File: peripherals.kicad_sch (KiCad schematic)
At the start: 71 parts, among them J801 TC2050-IDC-NL, J803 533980471, Q801 BSS138W-7-F, Q802 BSS138W-7-F, Q803 BSS138W-7-F, Q804 BSS138W-7-F, U801 TXB0108DQSR, U802 TXB0108DQSR, U803 PCAL6416AHF, U804 TXB0108DQSR, U805 AP22615, U806 AP22615, U807 74LVC1T45GM

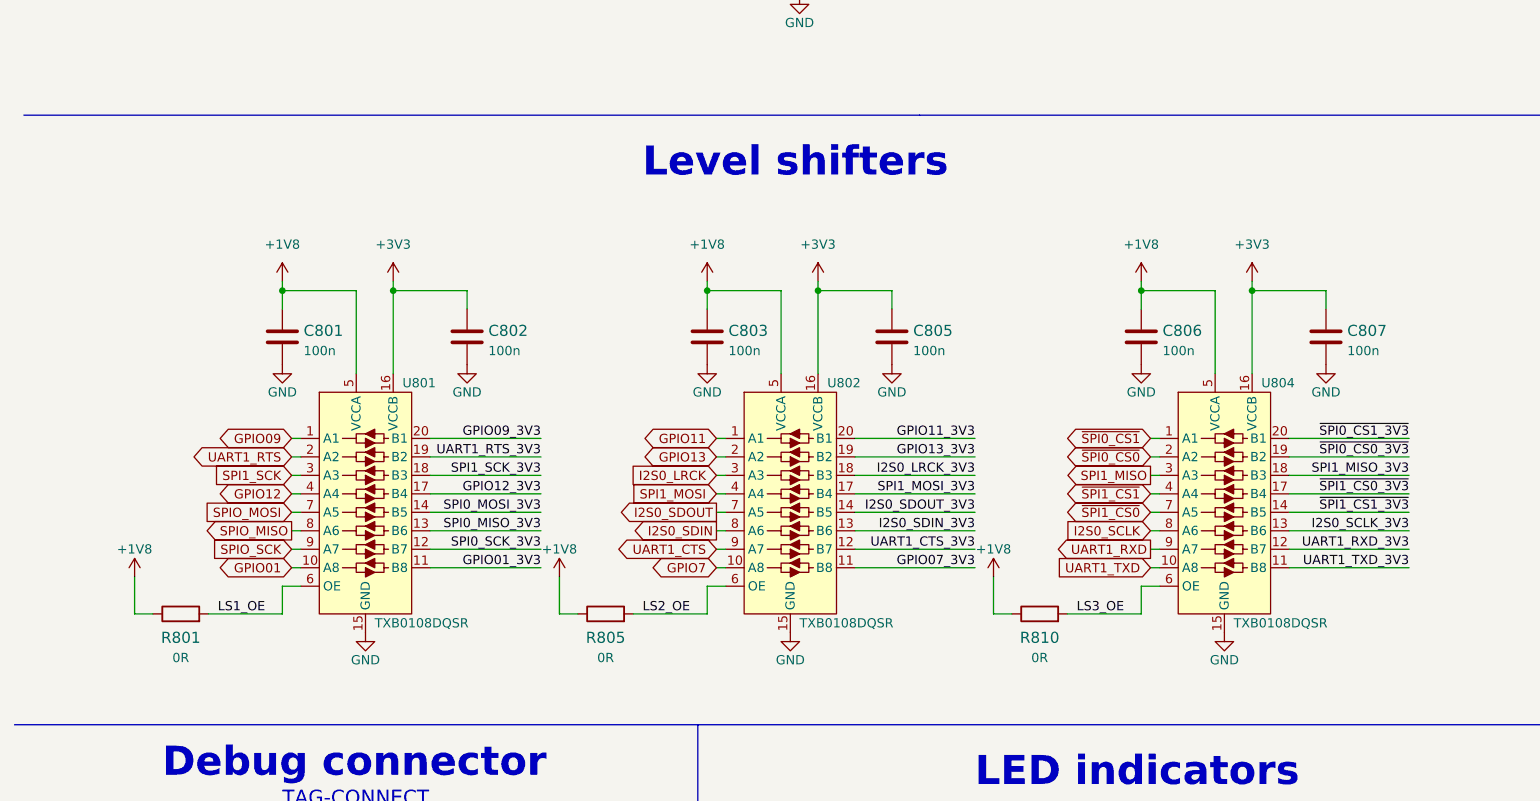
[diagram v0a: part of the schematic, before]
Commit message: Remove unused level shifters
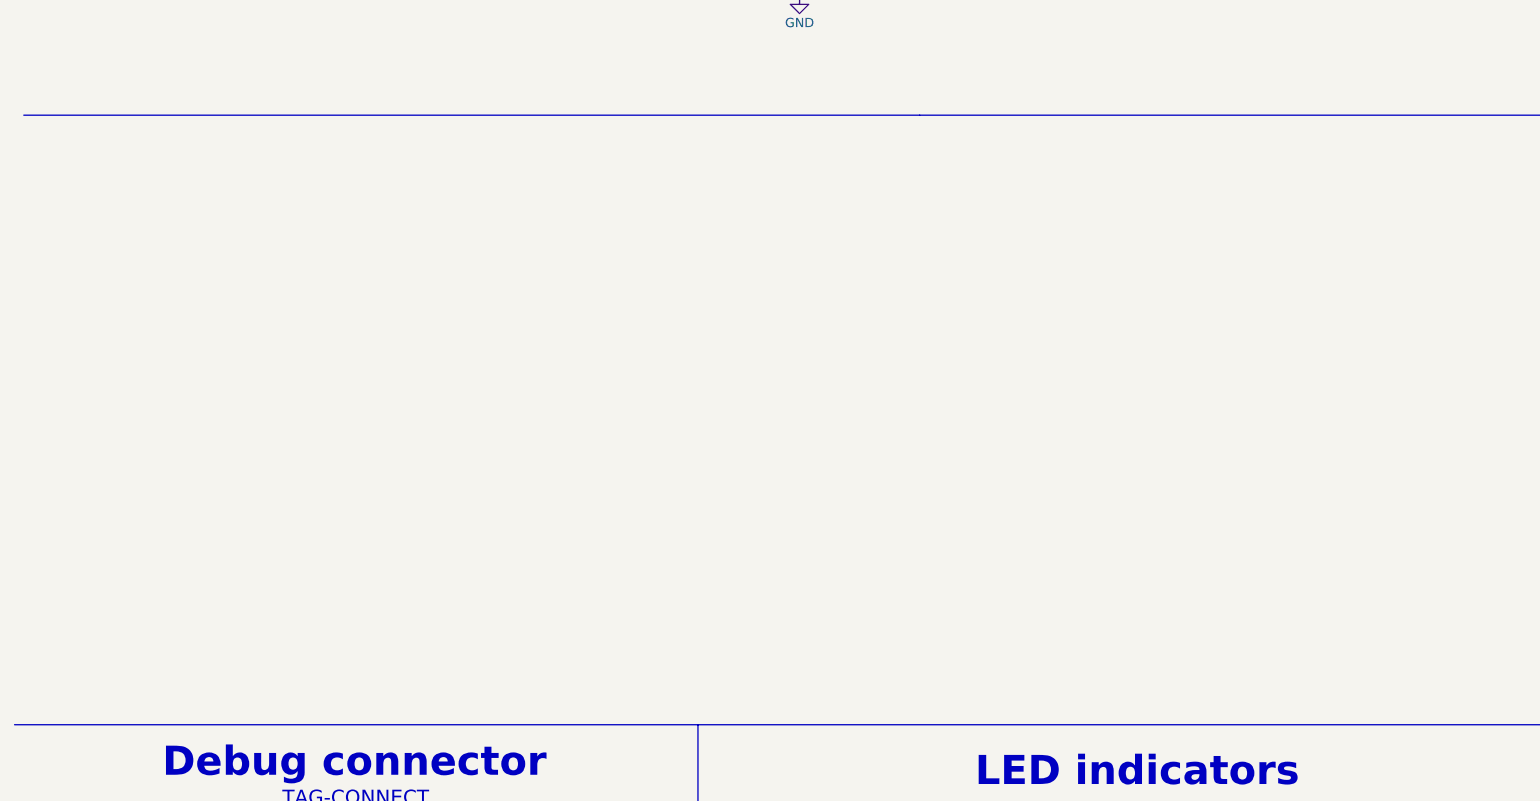
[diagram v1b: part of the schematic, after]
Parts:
- removed C801, C802, C803, C805, C806, C807: C_100n_0402, antmicro-footprints:0402-cap, symbol antmicroCapacitors0402:C_100n_0402
- removed R801, R805, R810: R_0R_0402, antmicro-footprints:0402-res, symbol antmicroResistors0402:R_0R_0402
- removed U801, U802, U804: TXB0108DQSR, antmicro-footprints:USON-20_2x4mm_P0.4mm, symbol antmicroLogicTranslatorsLevelShifters:TXB0108DQSR
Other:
- note removed: "Level shifters"

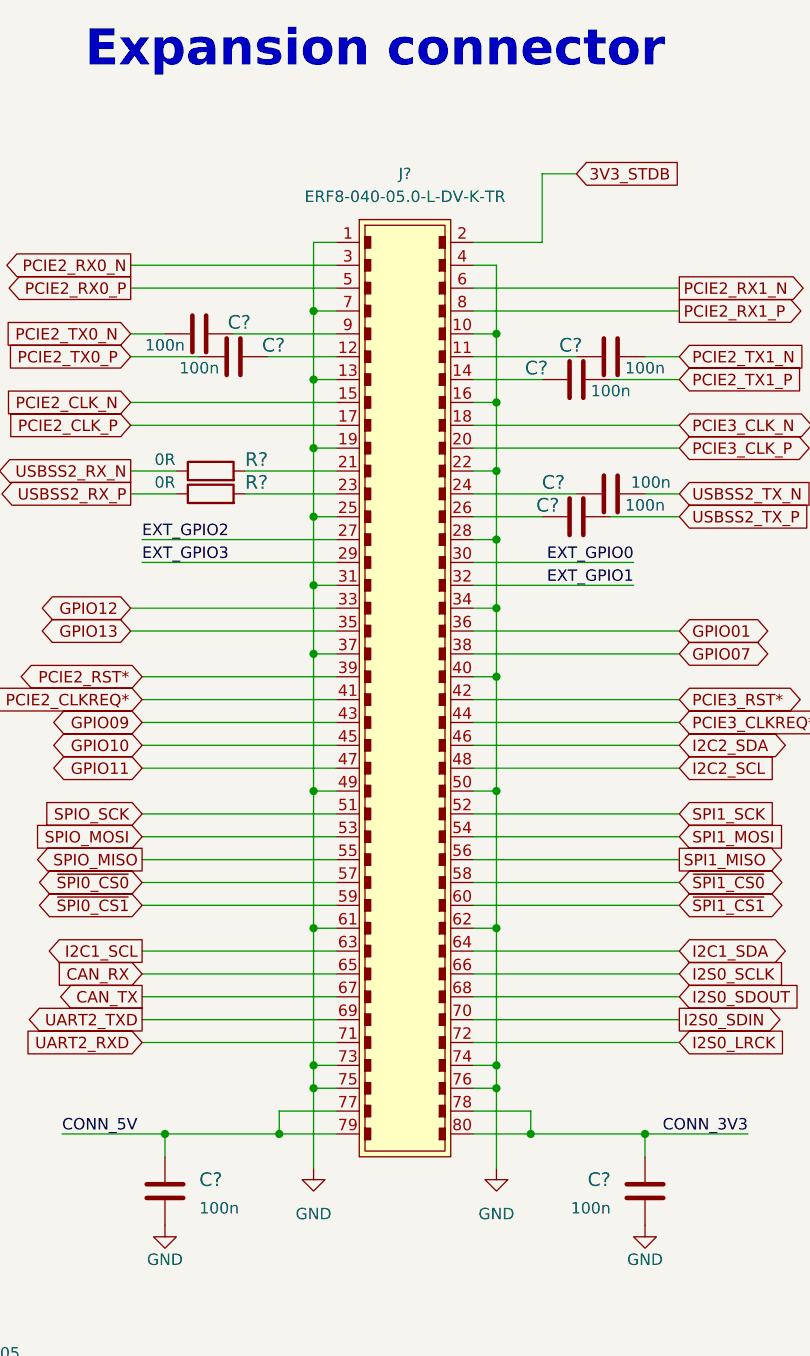
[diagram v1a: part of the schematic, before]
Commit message: Update expansion connector symbol, iport it to PCB
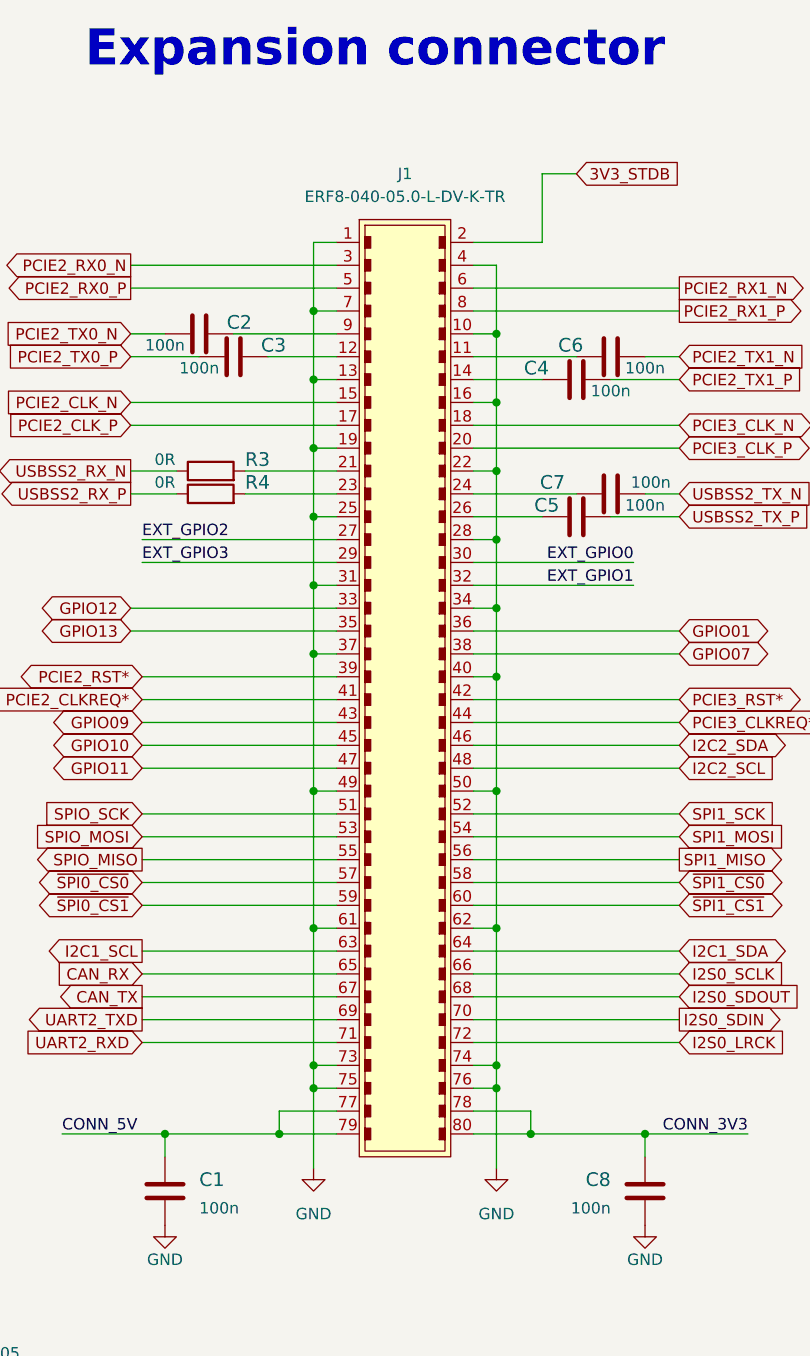
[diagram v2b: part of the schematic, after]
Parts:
- J1: renamed from J?; footprint antmicro-footprints:ERF8-XXX-XX.X-X-DV-XXXX-TR -> antmicro-footprints:ERF8-040-XX.X-X-DV-XX; Manufacturer (none) -> Samtec
- gave numbers to parts that had none: 10
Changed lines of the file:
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@@
   (symbol (lib_id "antmicroCapacitors0402:C_100n_0402") (at 341.63 71.12 270) (mirror x) (unit 1)
     (in_bom yes) (on_board yes)
-    (property "Reference" "C?" (id 0) (at 339.725 69.85 90)
+    (property "Reference" "C5" (id 0) (at 339.725 69.85 90)
       (effects (font (size 1.524 1.524)) (justify right))
     )
@@
   (symbol (lib_id "antmicroCapacitors0402:C_100n_0402") (at 341.63 55.88 270) (mirror x) (unit 1)
     (in_bom yes) (on_board yes)
-    (property "Reference" "C?" (id 0) (at 337.185 54.61 90)
+    (property "Reference" "C4" (id 0) (at 337.185 54.61 90)
       (effects (font (size 1.524 1.524)))
     )
@@
   (symbol (lib_id "antmicroCapacitors0402:C_100n_0402") (at 295.91 146.05 0) (mirror y) (unit 1)
     (in_bom yes) (on_board yes) (fields_autoplaced)
-    (property "Reference" "C?" (id 0) (at 299.72 144.78 0)
+    (property "Reference" "C1" (id 0) (at 299.72 144.78 0)
       (effects (font (size 1.524 1.524)) (justify right))
     )
@@
   (symbol (lib_id "antmicroCapacitors0402:C_100n_0402") (at 345.44 53.34 270) (mirror x) (unit 1)
     (in_bom yes) (on_board yes)
-    (property "Reference" "C?" (id 0) (at 340.995 52.07 90)
+    (property "Reference" "C6" (id 0) (at 340.995 52.07 90)
       (effects (font (size 1.524 1.524)))
     )
@@
   (symbol (lib_id "antmicroCapacitors0402:C_100n_0402") (at 349.25 146.05 0) (unit 1)
     (in_bom yes) (on_board yes) (fields_autoplaced)
-    (property "Reference" "C?" (id 0) (at 345.44 144.78 0)
+    (property "Reference" "C8" (id 0) (at 345.44 144.78 0)
       (effects (font (size 1.524 1.524)) (justify right))
     )
@@
   (symbol (lib_id "antmicroCapacitors0402:C_100n_0402") (at 299.72 50.8 90) (unit 1)
     (in_bom yes) (on_board yes)
-    (property "Reference" "C?" (id 0) (at 304.165 49.53 90)
+    (property "Reference" "C2" (id 0) (at 304.165 49.53 90)
       (effects (font (size 1.524 1.524)))
     )
@@
   (symbol (lib_id "power:GND") (at 349.25 149.86 0) (mirror y) (unit 1)
     (in_bom yes) (on_board yes)
-    (property "Reference" "#PWR?" (id 0) (at 349.25 156.21 0)
+    (property "Reference" "#PWR0162" (id 0) (at 349.25 156.21 0)
       (effects (font (size 1.27 1.27)) hide)
     )
@@
   (symbol (lib_id "antmicroResistors0402:R_0R_0402") (at 300.99 66.04 0) (unit 1)
     (in_bom yes) (on_board yes)
-    (property "Reference" "R?" (id 0) (at 304.8 64.77 0)
+    (property "Reference" "R3" (id 0) (at 304.8 64.77 0)
       (effects (font (size 1.524 1.524)) (justify left))
     )
@@
   (symbol (lib_id "power:GND") (at 312.42 143.51 0) (unit 1)
     (in_bom yes) (on_board yes) (fields_autoplaced)
-    (property "Reference" "#PWR?" (id 0) (at 312.42 149.86 0)
+    (property "Reference" "#PWR0160" (id 0) (at 312.42 149.86 0)
       (effects (font (size 1.27 1.27)) hide)
     )
@@
   (symbol (lib_id "antmicroResistors0402:R_0R_0402") (at 300.99 68.58 0) (unit 1)
     (in_bom yes) (on_board yes)
-    (property "Reference" "R?" (id 0) (at 304.8 67.31 0)
+    (property "Reference" "R4" (id 0) (at 304.8 67.31 0)
       (effects (font (size 1.524 1.524)) (justify left))
     )
@@
   (symbol (lib_id "antmicroCapacitors0402:C_100n_0402") (at 303.53 53.34 90) (unit 1)
     (in_bom yes) (on_board yes)
-    (property "Reference" "C?" (id 0) (at 307.975 52.07 90)
+    (property "Reference" "C3" (id 0) (at 307.975 52.07 90)
       (effects (font (size 1.524 1.524)))
     )
@@
   (symbol (lib_id "power:GND") (at 332.74 143.51 0) (unit 1)
     (in_bom yes) (on_board yes) (fields_autoplaced)
-    (property "Reference" "#PWR?" (id 0) (at 332.74 149.86 0)
+    (property "Reference" "#PWR0161" (id 0) (at 332.74 149.86 0)
       (effects (font (size 1.27 1.27)) hide)
     )
@@
   (symbol (lib_id "antmicroB2bConnectors:ERF8-040-05.0-L-DV-K-TR") (at 322.58 34.29 0) (unit 1)
     (in_bom yes) (on_board yes) (fields_autoplaced)
-    (property "Reference" "J?" (id 0) (at 322.58 33.02 0))
+    (property "Reference" "J1" (id 0) (at 322.58 33.02 0))
     (property "Value" "ERF8-040-05.0-L-DV-K-TR" (id 1) (at 322.58 35.56 0))
-    (property "Footprint" "antmicro-footprints:ERF8-XXX-XX.X-X-DV-XXXX-TR" (id 2) (at 322.58 34.29 0)
+    (property "Footprint" "antmicro-footprints:ERF8-040-XX.X-X-DV-XX" (id 2) (at 322.58 34.29 0)
       (effects (font (size 1.27 1.27)) hide)
     )
@@
     )
     (property "MPN" "ERF8-040-05.0-L-DV-K-TR" (id 4) (at 322.58 35.56 0)
+      (effects (font (size 1.27 1.27)) hide)
+    )
+    (property "Manufacturer" "Samtec" (id 5) (at 322.58 147.955 0)
       (effects (font (size 1.27 1.27)) hide)
     )
@@
   (symbol (lib_id "antmicroCapacitors0402:C_100n_0402") (at 345.44 68.58 270) (mirror x) (unit 1)
     (in_bom yes) (on_board yes)
-    (property "Reference" "C?" (id 0) (at 340.36 67.31 90)
+    (property "Reference" "C7" (id 0) (at 340.36 67.31 90)
       (effects (font (size 1.524 1.524)) (justify right))
     )
@@
   (symbol (lib_id "power:GND") (at 295.91 149.86 0) (unit 1)
     (in_bom yes) (on_board yes)
-    (property "Reference" "#PWR?" (id 0) (at 295.91 156.21 0)
-      (effects (font (size 1.27 1.27)) hide)
-    )
+    (property "Reference" "#PWR0159" (id 0) (at 295.91 156.21 0)
+      (effects (font (size 1.27 1.27)) hide)
+    )

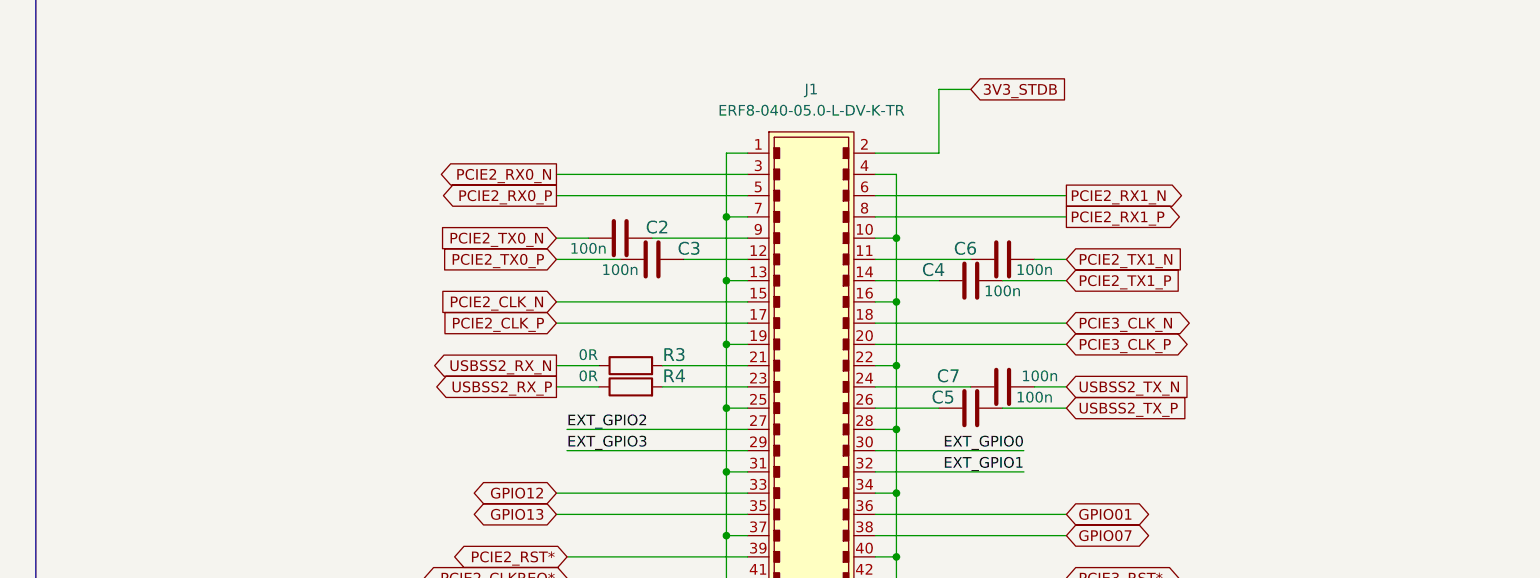
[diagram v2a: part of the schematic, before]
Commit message: Add R0 to expansion connector signals, add net labels
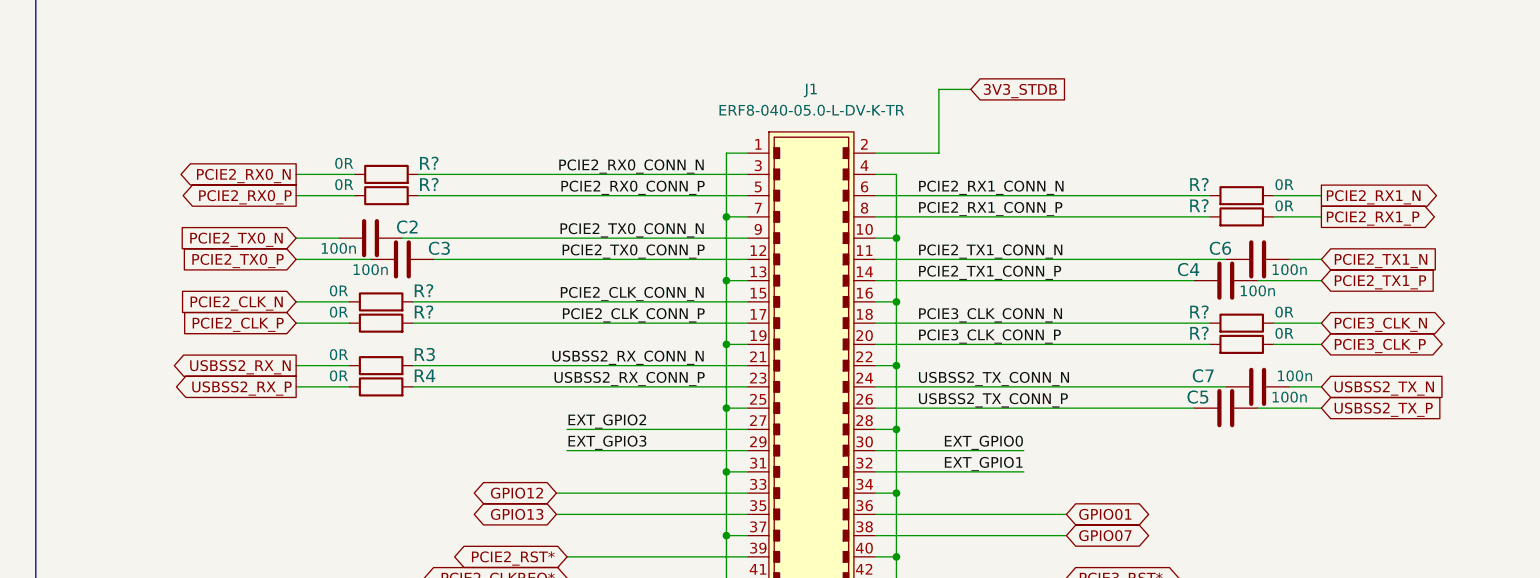
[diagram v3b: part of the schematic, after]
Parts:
- added R? (x8): R_0R_0402, antmicro-footprints:0402-res, symbol antmicroResistors0402:R_0R_0402
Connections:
- net PCIE2_CLK_N: now also R?.1; no longer J1.15
- net PCIE2_CLK_P: now also R?.1; no longer J1.17
- net PCIE2_RX0_N: now also R?.1; no longer J1.3
- net PCIE2_RX0_P: now also R?.1; no longer J1.5
- net PCIE2_RX1_N: now also R?.1; no longer J1.6
- net PCIE2_RX1_P: now also R?.1; no longer J1.8
- net PCIE3_CLK_N: now also R?.1; no longer J1.18
- net PCIE3_CLK_P: now also R?.1; no longer J1.20
- net USBSS2_TX_CONN_P: now reaches C5.2, J1.26
- net PCIE2_TX1_CONN_P: now reaches C4.2, J1.14
- net PCIE2_TX1_CONN_N: now reaches C6.2, J1.11
- net PCIE2_TX0_CONN_N: now reaches C2.2, J1.9
- net USBSS2_RX_CONN_N: now reaches J1.21, R3.2
- net USBSS2_RX_CONN_P: now reaches J1.23, R4.2
- net PCIE2_TX0_CONN_P: now reaches C3.2, J1.12
- net USBSS2_TX_CONN_N: now reaches C7.2, J1.24
- new net PCIE2_CLK_CONN_N: J1.15, R?.2
- new net PCIE2_CLK_CONN_P: J1.17, R?.2
- new net PCIE2_RX0_CONN_N: J1.3, R?.2
- new net PCIE2_RX0_CONN_P: J1.5, R?.2
- new net PCIE2_RX1_CONN_N: J1.6, R?.2
- new net PCIE2_RX1_CONN_P: J1.8, R?.2
- new net PCIE3_CLK_CONN_N: J1.18, R?.2
- new net PCIE3_CLK_CONN_P: J1.20, R?.2
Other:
- moved on the sheet: C2, C3, C4, C5, C6, C7, R3, R4
